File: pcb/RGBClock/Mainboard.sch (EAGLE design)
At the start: 102 parts, among them IC1 MCP23017SO, IC2 LT1763CS8-1.5, K1 G6K-2F, K2 G6K-2F, K3 G6K-2F, K4 G6K-2F, Q1 32.768KHz, U1 MAX6369KA+T, U10 NX3L1G384GW, U11 NX3L1G384GW, U13 DRV612PW, U14 2N7002-7-F, U15 2N7002-7-F, U16 2N7002-7-F, U17 2N7002-7-F, U2 TXS0102DCUR, U3 P82B96DR, U4 LM2675M-5.0, U5 DS1338Z-33+, U7 TPS71533DCKR, U8 NX3L1G384GW, U9 NX3L1G384GW, X2 43045-0400, X3 CON-LUMBERG_1503_09, X4 CON-LUMBERG_1503_09, X5 43045-0800, X6 ST-SMB-H

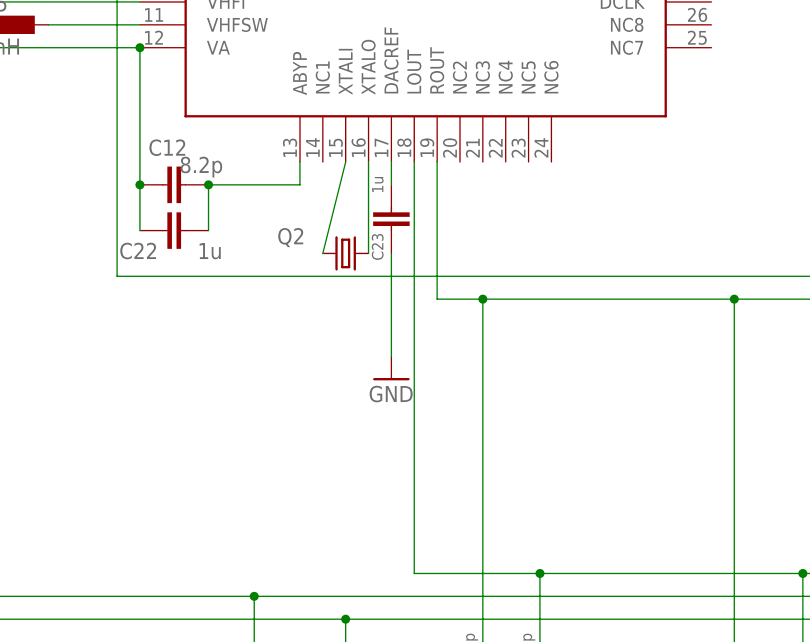
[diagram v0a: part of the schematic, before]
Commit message: met kleiner kristal
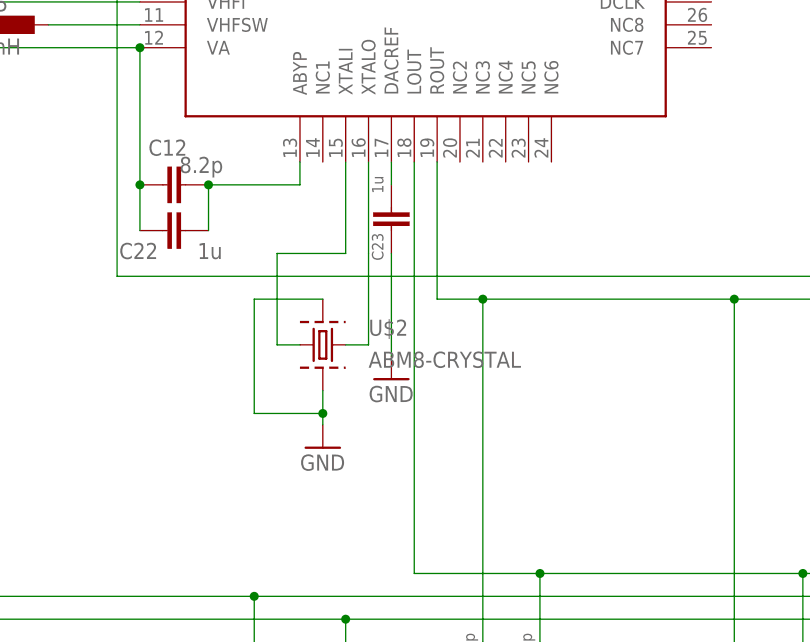
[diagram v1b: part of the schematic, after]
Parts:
- removed Q2: (no value), Mainboard:MAINBOARD_CRYSTAL_CRYSTALSM49
- added U$2: ABM8-CRYSTAL, Mainboard:ABM8-CRYSTAL
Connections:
- net GND: now also U$2.GND1, U$2.GND2
- net N$2: now also U$2.1; no longer Q2.1
- net N$26: now also U$2.2; no longer Q2.2
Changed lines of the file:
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@@
 <part name="CON1" library="Mainboard" deviceset="CON-HARTING_CON26" device=""/>
 <part name="B1" library="Mainboard" deviceset="MYCOMPONENTS_HU2032-LF" device="" value="HU2032-LF"/>
-<part name="Q2" library="Mainboard" deviceset="MAINBOARD_CRYSTAL_CRYSTAL" device="SM49"/>
 <part name="X6" library="Mainboard" deviceset="MAINBOARD_ST-SMB-H" device="" value="ST-SMB-H"/>
 <part name="IC2" library="Mainboard" deviceset="LINEAR-TECHNOLOGY_LT1763CS8" device="" technology="-1.5" value="LT1763CS8-1.5"/>
@@
 <part name="P+6" library="Mainboard" deviceset="SUPPLY1_+24V" device="" value="+1.8V"/>
 <part name="U$6" library="Mainboard" deviceset="SI4684-MYSMD" device=""/>
+<part name="GND16" library="Mainboard" deviceset="SUPPLY1_GND" device="" value="GND"/>
+<part name="U$2" library="Mainboard" deviceset="ABM8-CRYSTAL" device=""/>
 </parts>
 <sheets>
@@
 <attribute name="VALUE" x="68.58" y="-129.54" size="1.778" layer="96" rot="R90"/>
 </instance>
-<instance part="Q2" gate="G$1" x="88.9" y="35.56" smashed="yes">
-<attribute name="NAME" x="81.28" y="36.576" size="1.778" layer="95"/>
-<attribute name="VALUE" x="91.44" y="33.02" size="1.778" layer="96"/>
-</instance>
 <instance part="X6" gate="G1" x="1.27" y="96.52" smashed="yes">
 <attribute name="VALUE" x="-6.35" y="101.6" size="1.778" layer="96"/>
@@
 </instance>
 <instance part="U$6" gate="A" x="104.14" y="76.2" smashed="yes"/>
+<instance part="GND16" gate="1" x="86.36" y="13.97" smashed="yes">
+<attribute name="VALUE" x="83.82" y="11.43" size="1.778" layer="96"/>
+</instance>
+<instance part="U$2" gate="A" x="86.36" y="25.4" smashed="yes">
+<attribute name="NAME" x="91.44" y="26.416" size="1.778" layer="95"/>
+<attribute name="VALUE" x="91.44" y="22.86" size="1.778" layer="96"/>
+</instance>
 </instances>
 <busses>
@@
 <wire x1="143.51" y1="68.58" x2="129.54" y2="68.58" width="0.1524" layer="91"/>
 <junction x="143.51" y="66.04"/>
+</segment>
+<segment>
+<pinref part="GND16" gate="1" pin="GND"/>
+<wire x1="86.36" y1="17.78" x2="86.36" y2="16.51" width="0.1524" layer="91"/>
+<wire x1="78.74" y1="30.48" x2="78.74" y2="17.78" width="0.1524" layer="91"/>
+<wire x1="78.74" y1="17.78" x2="86.36" y2="17.78" width="0.1524" layer="91"/>
+<pinref part="U$2" gate="A" pin="GND1"/>
+<wire x1="78.74" y1="30.48" x2="86.36" y2="30.48" width="0.1524" layer="91"/>
+<pinref part="U$2" gate="A" pin="GND2"/>
+<wire x1="86.36" y1="20.32" x2="86.36" y2="17.78" width="0.1524" layer="91"/>
+<junction x="86.36" y="17.78"/>
 </segment>
 </net>
@@
 </segment>
 </net>
-<net name="N$2" class="4">
-<segment>
-<pinref part="Q2" gate="G$1" pin="1"/>
-<wire x1="88.9" y1="45.72" x2="86.36" y2="35.56" width="0.1524" layer="91"/>
-<pinref part="U$6" gate="A" pin="XTALI"/>
-</segment>
-</net>
 <net name="N$26" class="4">
 <segment>
 <wire x1="91.44" y1="45.72" x2="91.44" y2="35.56" width="0.1524" layer="91"/>
-<pinref part="Q2" gate="G$1" pin="2"/>
 <pinref part="U$6" gate="A" pin="XTALO"/>
+<wire x1="91.44" y1="35.56" x2="91.44" y2="25.4" width="0.1524" layer="91"/>
+<pinref part="U$2" gate="A" pin="2"/>
+<wire x1="91.44" y1="25.4" x2="88.9" y2="25.4" width="0.1524" layer="91"/>
 </segment>
 </net>
@@
 </segment>
 </net>
+<net name="N$2" class="0">
+<segment>
+<pinref part="U$6" gate="A" pin="XTALI"/>
+<wire x1="88.9" y1="45.72" x2="88.9" y2="35.56" width="0.1524" layer="91"/>
+<wire x1="88.9" y1="35.56" x2="81.28" y2="35.56" width="0.1524" layer="91"/>
+<wire x1="81.28" y1="35.56" x2="81.28" y2="25.4" width="0.1524" layer="91"/>
+<pinref part="U$2" gate="A" pin="1"/>
+<wire x1="81.28" y1="25.4" x2="83.82" y2="25.4" width="0.1524" layer="91"/>
+</segment>
+</net>

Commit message: As send to JCLPCB
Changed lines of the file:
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@@
 </instance>
 <instance part="U$2" gate="A" x="86.36" y="25.4" smashed="yes">
-<attribute name="NAME" x="91.44" y="26.416" size="1.778" layer="95"/>
-<attribute name="VALUE" x="91.44" y="22.86" size="1.778" layer="96"/>
+<attribute name="NAME" x="73.66" y="26.416" size="1.778" layer="95"/>
+<attribute name="VALUE" x="58.42" y="22.86" size="1.778" layer="96"/>
 </instance>
 </instances>

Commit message: -dab documentation -bom Mainboard.b#1 -small changes pcb
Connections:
- removed net N$62: U$6.SMODE
- net +3V3: now also U$6.SMODE
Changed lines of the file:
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@@
 <junction x="261.62" y="114.3"/>
+</segment>
+<segment>
+<pinref part="U$6" gate="A" pin="SMODE"/>
+<pinref part="+3V9" gate="G$1" pin="+3V3"/>
+<wire x1="66.04" y1="76.2" x2="48.26" y2="76.2" width="0.1524" layer="91"/>
+<wire x1="48.26" y1="76.2" x2="48.26" y2="81.28" width="0.1524" layer="91"/>
 </segment>
 </net>
@@
 <segment>
 <wire x1="111.76" y1="99.06" x2="111.76" y2="101.6" width="0.1524" layer="91"/>
-<pinref part="C28" gate="G$1" pin="2"/>
 <wire x1="111.76" y1="101.6" x2="111.76" y2="106.68" width="0.1524" layer="91"/>
 <wire x1="111.76" y1="106.68" x2="111.76" y2="107.95" width="0.1524" layer="91"/>
-<wire x1="116.84" y1="107.95" x2="111.76" y2="107.95" width="0.1524" layer="91"/>
 <pinref part="C29" gate="G$1" pin="2"/>
 <wire x1="116.84" y1="101.6" x2="111.76" y2="101.6" width="0.1524" layer="91"/>
 <junction x="111.76" y="101.6"/>
 <pinref part="P+6" gate="1" pin="+24V"/>
-<wire x1="111.76" y1="111.76" x2="111.76" y2="107.95" width="0.1524" layer="91"/>
+<wire x1="111.76" y1="111.76" x2="111.76" y2="109.22" width="0.1524" layer="91"/>
 <pinref part="U$6" gate="A" pin="VCORE"/>
+<pinref part="C28" gate="G$1" pin="2"/>
+<wire x1="111.76" y1="109.22" x2="111.76" y2="107.95" width="0.1524" layer="91"/>
+<wire x1="116.84" y1="107.95" x2="111.76" y2="107.95" width="0.1524" layer="91"/>
+<wire x1="111.76" y1="107.95" x2="111.76" y2="109.22" width="0.1524" layer="91"/>
+<junction x="111.76" y="109.22"/>
 </segment>
 </net>
@@
 </segment>
 </net>
-<net name="N$62" class="4">
-<segment>
-<pinref part="+3V9" gate="G$1" pin="+3V3"/>
-<wire x1="48.26" y1="81.28" x2="48.26" y2="76.2" width="0.1524" layer="91"/>
-<wire x1="48.26" y1="76.2" x2="66.04" y2="76.2" width="0.1524" layer="91"/>
-<pinref part="U$6" gate="A" pin="SMODE"/>
-</segment>
-</net>

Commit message: Voor optimalisatie (v2.1)
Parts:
- removed IC2: LT1763CS8-1.5, Mainboard:LINEAR-TECHNOLOGY_LT1763CS8-1.5
- removed TP-5V: TESTPAD_TPSTP10SQ, Mainboard:TESTPAD_TPSTP10SQ
- removed TP6, TP7: TESTPAD_TPTP07SQ, Mainboard:TESTPAD_TPTP07SQ
- removed U7: TPS71533DCKR, Mainboard:TEXAS_TPS71533DCKR
- removed X3, X4: CON-LUMBERG_1503_09, Mainboard:CON-LUMBERG_1503_09
- added C15, C30: 100n, Mainboard:RCL_C-EUC0805
- added C18, C31, C32, C33, C34, C35: 1u, Mainboard:RCL_C-EUC0805
- added TP1, TP8, TP9: PTR1PAD1-13, testpad:PTR1PAD1-13
- added U$10: TPS79133, Mainboard:TPS79133
- added U$11, U$12: FC68131FC68131, Mainboard:FC68131FC68131
- added U$7, U$8, U$9: TPS79118, Mainboard:TPS79118
- C14: value 0,47u -> 1u
- C4: value 10n -> 1u
- D1: value MUR480ERLG -> B340-13-F; device Mainboard:DIODE_MUR150RL -> Mainboard:DIODE_DIODE-DO-214AC
- LED1: value 5mm Led -> (none); device Mainboard:LED_LED5MM -> led:LEDCHIP-LED0805
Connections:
- removed net +1.8V: C11.1, C12.1, C13.1, C22.1, C28.2, C29.2, C4.1, IC2.OUT, IC2.SENSE, U$6.VA, U$6.VCORE, U$6.VMEM
- new net +1.8-MEM: C11.1, C13.1, C31.1, U$6.VMEM, U$9.OUT
- new net +1.8-VA: C12.1, C22.1, C4.1, U$6.VA, U$7.OUT
- new net +1.8-VCORE: C18.1, C28.2, C29.2, U$6.VCORE, U$8.OUT
- new net N$39: C33.2, C6.1, U$7.BYP
- new net N$62: C30.1, C35.2, U$9.BYP
- new net N$65: C32.2, C7.1, U$10.BYP
- net +3V3: now also U$10.OUT; no longer U7.OUT
- net +5V: now also C32.1, C33.1, C34.1, C35.1, TP1.TP, U$10.IN, U$7.IN, U$8.IN, U$9.IN; no longer C6.1, C7.1, IC2.!SHDN, IC2.IN, TP-5V.PP, U7.IN
- net GND: now also C15.2, C18.2, C30.2, C31.2, C4.2, CON1.14, CON1.20, CON1.25, CON1.9, U$10.EN, U$10.GND, U$11.GND, U$12.GND, U$7.EN, U$7.GND, U$8.EN, U$8.GND, U$9.EN, U$9.GND; no longer IC2.GND@1, IC2.GND@2, IC2.GND@3, U7.GND, X3.1, X4.1
- net N$4: now also CON1.4
- net N$40: now also U$12.LEFT; no longer X4.2, X4.4
- net N$44: now also U$12.RIGHT; no longer X4.3, X4.5
- net N$47: now also U$11.LEFT; no longer X3.2, X3.4
- net N$49: now also U$11.RIGHT; no longer X3.3, X3.5
- net N$58: now also C15.1, C34.2, U$8.BYP; no longer C4.2, IC2.BYP
- net SCL: now also TP8.TP; no longer TP6.TP
- net SDA: now also TP9.TP; no longer TP7.TP
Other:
- moved on the sheet: C14, C4

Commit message: as send to Jclpcb (ver 1.3)
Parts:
- removed C1: 100n, Mainboard:RCL_C-EUC0805
- removed C5: 594D686X0010C2T, Mainboard:MYCOMPONENTS_594D686X0010C2T
- removed D4: B130-13-F, Mainboard:DIODE_DIODE-DO-214AC
- removed L1: SRR1240-680M, Mainboard:BOURNS_BY_ELEMENT14_BATCH_1_SRR1240-680M
- removed R14: A2-1, Mainboard:RESISTOR_R-EU_R0402:1
- removed R15: A2-0, Mainboard:RESISTOR_R-EU_R0402:1
- removed R16: A1-1, Mainboard:RESISTOR_R-EU_R0402:1
- removed R17: A1-0, Mainboard:RESISTOR_R-EU_R0402:1
- removed R18: A0-1, Mainboard:RESISTOR_R-EU_R0402:1
- removed R19: A0-0, Mainboard:RESISTOR_R-EU_R0402:1
- removed U4: LM2675M-5.0, Mainboard:TEXAS_LM2675M-5.0
- added C36: 100n, Mainboard:RCL_C-EUC0805
- added IC2: R-78B5.0-2.0, linear:7805TV
- added R20: 3K48, rcl:R-EU_M0805
- added SJ1: A2, jumper:SJ2W
- added SJ2: A1, jumper:SJ2W
- added SJ3: A0, jumper:SJ2W
- added U$13: SST26VF032B, Mainboard:SST26VF032B
- C2: value 4,7u -> 10u
- C3: value 10n -> 10u; device Mainboard:RCL_C-EUC0805 -> Mainboard:RCL_C-EUC1206
- CON1: device Mainboard:CON-HARTING_CON26 -> con-harting:CON26
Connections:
- removed net N$42: IC1.A1, R16.1, R17.2
- removed net N$43: IC1.A2, R14.1, R15.2
- new net N$71: U$13.SCK, U$6.NVSCLK
- new net N$72: U$13.SO/SOI1, U$6.NVMISO
- new net N$73: R20.2, U$13.CE, U$6.NVSSB
- new net N$74: U$13.SI/SIO0, U$6.NVMOSI
- net +3V3: now also C36.1, R20.1, SJ1.1, SJ2.1, SJ3.1, U$13.HOLD/SIO3, U$13.VCC, U$13.WP#/SIO2; no longer R14.2, R16.2, R18.2
- net +5V: now also C3.1, IC2.VO; no longer C5.1, L1.1, U4.FB
- net GND: now also C3.2, C32.2, C33.2, C34.2, C35.2, C36.2, IC2.GND, SJ1.3, SJ2.3, SJ3.3, U$13.GND; no longer C1.2, C5.2, D4.A, R15.1, R17.1, R19.1, U4.GND
- net N$10: now also IC1.A2, SJ1.2; no longer C3.1, U4.CB
- net N$11: now also IC1.A1, SJ2.2; no longer C3.2, D4.C, L1.2, U4.VSW
- net N$39: no longer C33.2
- net N$41: now also SJ3.2; no longer R18.1, R19.2
- net N$58: no longer C34.2
- net N$62: no longer C35.2
- net N$65: no longer C32.2
- net VCC: now also IC2.VI; no longer C1.1, U4.VIN
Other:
- note added: "3: SDA 5: SCL"
- note removed: "3: SDA 4: SCL"
- moved on the sheet: C15, C3, C30, C33, C34, C6, C7, C8, CON1, JP2, TP1, U$1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

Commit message: Send to jclpcb
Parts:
- added R14: 10k, rcl:R-EU_M0805
- added SPI: TXS0104E, Mainboard:TXS0104E
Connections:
- new net CE0: CON1.24, SPI.A4
- new net MISO: CON1.21, SPI.A2
- new net MOSI: CON1.19, SPI.A1
- new net SCLK: CON1.23, SPI.A3
- new net SI-MISO: SPI.B2, U$6.MISO
- new net SI_MOSI: SPI.B1, U$6.MOSI
- new net SI_SCLK: SPI.B3, U$6.SCLK
- new net SI_SSB: SPI.B4, U$6.SSB
- net +3V3: now also SPI.VCCB; no longer U$6.SMODE
- net GND: now also R14.1, SPI.GND, U$6.SMODE; no longer U$6.MISO, U$6.SSB
- net N$8: now also R14.2, SPI.OE, SPI.VCCA
- net SCL: no longer U$6.SCLK
- net SDA: no longer U$6.MOSI
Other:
- note added: "TXS0104E"
- moved on the sheet: C24, C25, CON1, JP1, JP2, R8, R9, U1

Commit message: - some comments
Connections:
- net N$71 renamed NVSCLK
- net N$72 renamed NVMISO
- net N$73 renamed NVSSB
- net N$74 renamed NVMOSI
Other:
- note added: "SQW and VCC switched !!!"
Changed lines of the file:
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@@
 <text x="-74.34" y="50" size="1.778" layer="95">SCL</text>
 <text x="-60.96" y="-99.06" size="1.778" layer="91">TXS0104E</text>
+<text x="83.82" y="-96.52" size="1.778" layer="91">SQW and VCC switched !!!</text>
 </plain>
 <instances>
@@
 </segment>
 </net>
-<net name="N$71" class="0">
+<net name="NVSCLK" class="0">
 <segment>
 <pinref part="U$13" gate="G$1" pin="SCK"/>
@@
 <pinref part="U$6" gate="A" pin="NVSCLK"/>
 <wire x1="60.96" y1="83.82" x2="66.04" y2="83.82" width="0.1524" layer="91"/>
-</segment>
-</net>
-<net name="N$73" class="0">
+<label x="45.72" y="88.9" size="1.778" layer="95"/>
+</segment>
+</net>
+<net name="NVSSB" class="0">
 <segment>
 <pinref part="U$13" gate="G$1" pin="CE"/>
@@
 <pinref part="R20" gate="G$1" pin="2"/>
 <wire x1="-33.02" y1="99.06" x2="-33.02" y2="101.6" width="0.1524" layer="91"/>
-</segment>
-</net>
-<net name="N$74" class="0">
+<label x="45.72" y="109.22" size="1.778" layer="95"/>
+</segment>
+</net>
+<net name="NVMOSI" class="0">
 <segment>
 <pinref part="U$13" gate="G$1" pin="SI/SIO0"/>
@@
 <pinref part="U$6" gate="A" pin="NVMOSI"/>
 <wire x1="83.82" y1="101.6" x2="83.82" y2="99.06" width="0.1524" layer="91"/>
-</segment>
-</net>
-<net name="N$72" class="0">
+<label x="45.72" y="101.6" size="1.778" layer="95"/>
+</segment>
+</net>
+<net name="NVMISO" class="0">
 <segment>
 <pinref part="U$13" gate="G$1" pin="SO/SOI1"/>
@@
 <wire x1="-17.78" y1="114.3" x2="86.36" y2="114.3" width="0.1524" layer="91"/>
 <wire x1="86.36" y1="114.3" x2="86.36" y2="99.06" width="0.1524" layer="91"/>
-</segment>
-</net>
+<label x="45.72" y="114.3" size="1.778" layer="95"/>
+</segment>
+</net>
